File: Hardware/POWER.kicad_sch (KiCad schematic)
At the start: 91 parts, among them J201 Battery, J202 POWER IN, J203 5V_SEL, J204 E5V, SW201 START, U201 AP2112K-3.3, U203 AP2151W, U204 AP2112K-3.3, U205 AP2112K-1.8, U206 AP2112K-3.3, U207 AP2112K-3.3, U209 AP2171W

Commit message: Checkpoint
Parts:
- added R202, R210: 100K, Resistor_SMD:R_0805_2012Metric, symbol Device:R_Small
- R233: renamed from R227; value 100 -> 100R
- renumbered R202 to R203, R203 to R204, R204 to R205, R207 to R208, R208 to R209, R209 to R211, R210 to R212, R211 to R213, R212 to R214, R213 to R215, R214 to R216, R215 to R217, R217 to R218, R216 to R219, R234 to R220, R235 to R221, R236 to R222, R237 to R223, R218 to R224, R219 to R225, R220 to R226, R221 to R227, R222 to R228, R223 to R229, R225 to R230, R224 to R231, R226 to R232, R228 to R234, R229 to R235, R230 to R236, R231 to R237, R232 to R238, R233 to R239, U209 to U208
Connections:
- net D1_5V: now also R202.2, R210.2
- net D5_EN: now also R202.1
- net SERVO_5V_AUX_EN: now also R210.1

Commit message: Checkpoint
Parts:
- removed J201: Battery, Connector_PinHeader_2.54mm:PinHeader_1x07_P2.54mm_Vertical, symbol Connector_Generic:Conn_01x07
- removed R214, R216, R218, R219: 100K, Resistor_SMD:R_0805_2012Metric, symbol Device:R_Small
- removed R224, R225, R226, R227, R228: 10K, Resistor_SMD:R_0603_1608Metric, symbol Device:R_Small
- added C223, C224: 1nF, Capacitor_SMD:C_0603_1608Metric, symbol Device:C_Small
- added C? (x2): 100nF, Capacitor_SMD:C_0603_1608Metric, symbol Device:C_Small
- added R211, R220, R221: 10K, Resistor_SMD:R_0603_1608Metric, symbol Device:R_Small
- added R222, R223: 15K, Resistor_SMD:R_1206_3216Metric, symbol Device:R_Small
- added TP207, TP209: ~, TestPoint:TestPoint_Pad_D2.0mm, symbol Connector:TestPoint
- added U208, U209: ACS714xLCTR-50A, Package_SO:SOIC-8_3.9x4.9mm_P1.27mm, symbol Sensor_Current:ACS714xLCTR-50A
- R212, R213, R215: value 100K -> 10K; footprint Resistor_SMD:R_0805_2012Metric -> Resistor_SMD:R_0603_1608Metric
- renumbered C220 to C222, C221 to C225, C222 to C226, J203 to J201, J204 to J202, J202 to J203, R217 to R210, R229 to R214, R230 to R216, R231 to R217, R210 to R218, R211 to R219, R220 to R224, R221 to R225, R222 to R226, R223 to R227, R232 to R228, R233 to R229, R234 to R230, R235 to R231, R236 to R232, R237 to R233, R238 to R234, R239 to R235, TP207 to TP210, U208 to U210
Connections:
- net BATT_S2 is gone; now on net D1_5V: R213.1
- net BATT_S4 is gone; now on net MEAS_SERVO: R215.1
- net BATT_S6 is gone; now on net PWR_IN: R210.1
- net MEAS_S1 is gone; now on net SERVO_5V5: R212.1
- net MEAS_S2 is gone; now on net MEAS_D1_5V: R213.2
- net MEAS_S4 is gone; now on net GND: R215.2
- net D1_5V: now also C?.2, C?.2, U208.3 (IP-), U208.4 (IP-), U208.8 (VCC), U209.8 (VCC); no longer J201.1 (Pin_1), J201.3 (Pin_3), J201.5 (Pin_5)
- net GND: now also C223.2, C224.2, C?.1, C?.1, R222.2, R223.2, U208.5 (GND), U209.5 (GND)
- net MEAS_SERVO: now also R211.2; no longer R216.1
- net SERVO_5V5: now also R211.1, U209.3 (IP-), U209.4 (IP-)
- net BATT_S1 renamed MEAS_D5_5V
- net MEAS_D5_5V: now also R216.1
- net MEAS_S6 renamed MEAS_POWER_IN
- new net: C224.1, U209.6 (FILTER)
- new net: J201.1 (Pin_1), J201.3 (Pin_3), J201.5 (Pin_5), TP207.1, U208.1 (IP+), U208.2 (IP+)
- new net: R221.1, U209.7 (VIOUT)
- new net: C223.1, U208.6 (FILTER)
- new net: R220.1, U208.7 (VIOUT)
- new net MEAS_I_D1_5V: R220.2, R222.1
- new net MEAS_I_SERVO_5V5: R221.2, R223.1
- new net SERVO_ESC: TP209.1, U209.1 (IP+), U209.2 (IP+)
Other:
- moved on the sheet: D203, D204, D205, D206, D207, D208, J201, J202, J203, Q?, R210, R214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

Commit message: Checkpoint
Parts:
- TP201, TP202, TP203, TP204, TP205, TP206, TP207, TP208, TP209, TP210: footprint TestPoint:TestPoint_Pad_D2.0mm -> TestPoint:TestPoint_Pad_D1.0mm
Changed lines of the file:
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@@
       (effects (font (size 1.27 1.27)) hide)
     )
-    (property "Footprint" "TestPoint:TestPoint_Pad_D2.0mm" (at 109.22 213.36 0)
+    (property "Footprint" "TestPoint:TestPoint_Pad_D1.0mm" (at 109.22 213.36 0)
       (effects (font (size 1.27 1.27)) hide)
     )
@@
       (effects (font (size 1.27 1.27)) hide)
     )
-    (property "Footprint" "TestPoint:TestPoint_Pad_D2.0mm" (at 109.22 142.24 0)
+    (property "Footprint" "TestPoint:TestPoint_Pad_D1.0mm" (at 109.22 142.24 0)
       (effects (font (size 1.27 1.27)) hide)
     )
@@
       (effects (font (size 1.27 1.27)) hide)
     )
-    (property "Footprint" "TestPoint:TestPoint_Pad_D2.0mm" (at 48.26 213.36 0)
+    (property "Footprint" "TestPoint:TestPoint_Pad_D1.0mm" (at 48.26 213.36 0)
       (effects (font (size 1.27 1.27)) hide)
     )
@@
       (effects (font (size 1.27 1.27)) hide)
     )
-    (property "Footprint" "TestPoint:TestPoint_Pad_D2.0mm" (at 109.22 172.72 0)
+    (property "Footprint" "TestPoint:TestPoint_Pad_D1.0mm" (at 109.22 172.72 0)
       (effects (font (size 1.27 1.27)) hide)
     )
@@
       (effects (font (size 1.27 1.27)) hide)
     )
-    (property "Footprint" "TestPoint:TestPoint_Pad_D2.0mm" (at 154.94 109.22 0)
+    (property "Footprint" "TestPoint:TestPoint_Pad_D1.0mm" (at 154.94 109.22 0)
       (effects (font (size 1.27 1.27)) hide)
     )
@@
       (effects (font (size 1.27 1.27)) hide)
     )
-    (property "Footprint" "TestPoint:TestPoint_Pad_D2.0mm" (at 88.9 251.46 0)
+    (property "Footprint" "TestPoint:TestPoint_Pad_D1.0mm" (at 88.9 251.46 0)
       (effects (font (size 1.27 1.27)) hide)
     )
@@
       (effects (font (size 1.27 1.27)) hide)
     )
-    (property "Footprint" "TestPoint:TestPoint_Pad_D2.0mm" (at 114.3 99.06 0)
+    (property "Footprint" "TestPoint:TestPoint_Pad_D1.0mm" (at 114.3 99.06 0)
       (effects (font (size 1.27 1.27)) hide)
     )
@@
       (effects (font (size 1.27 1.27)) hide)
     )
-    (property "Footprint" "TestPoint:TestPoint_Pad_D2.0mm" (at 215.9 251.46 0)
+    (property "Footprint" "TestPoint:TestPoint_Pad_D1.0mm" (at 215.9 251.46 0)
       (effects (font (size 1.27 1.27)) hide)
     )
@@
       (effects (font (size 1.27 1.27)) hide)
     )
-    (property "Footprint" "TestPoint:TestPoint_Pad_D2.0mm" (at 152.4 53.34 0)
+    (property "Footprint" "TestPoint:TestPoint_Pad_D1.0mm" (at 152.4 53.34 0)
       (effects (font (size 1.27 1.27)) hide)
     )
@@
       (effects (font (size 1.27 1.27)) hide)
     )
-    (property "Footprint" "TestPoint:TestPoint_Pad_D2.0mm" (at 152.4 63.5 0)
-      (effects (font (size 1.27 1.27)) hide)
-    )
+    (property "Footprint" "TestPoint:TestPoint_Pad_D1.0mm" (at 152.4 63.5 0)
+      (effects (font (size 1.27 1.27)) hide)
+    )

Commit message: Checkpoint routing
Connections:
- net SERVO_5V5: now also TP209.1, U209.1 (IP+), U209.2 (IP+); no longer U209.3 (IP-), U209.4 (IP-)
- net SERVO_ESC: now also U209.3 (IP-), U209.4 (IP-); no longer TP209.1, U209.1 (IP+), U209.2 (IP+)
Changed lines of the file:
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@@
     (effects (font (size 1.27 1.27)) (justify right))
   )
-  (hierarchical_label "SERVO_ESC" (shape passive) (at 157.48 109.22 180) (fields_autoplaced)
+  (hierarchical_label "SERVO_ESC" (shape passive) (at 157.48 119.38 180) (fields_autoplaced)
     (effects (font (size 1.27 1.27)) (justify right))
   )
@@
     (effects (font (size 1.27 1.27)) (justify left))
   )
-  (hierarchical_label "SERVO_5V5" (shape passive) (at 157.48 119.38 180) (fields_autoplaced)
+  (hierarchical_label "SERVO_5V5" (shape passive) (at 157.48 109.22 180) (fields_autoplaced)
     (effects (font (size 1.27 1.27)) (justify right))
   )

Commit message: Finalize schematic and some more routing
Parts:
- R229: value 100R -> 150R; footprint Resistor_SMD:R_0805_2012Metric -> Resistor_SMD:R_0603_1608Metric
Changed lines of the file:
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@@
   (junction (at 73.66 66.04) (diameter 0) (color 0 0 0 0)
   )
+  (junction (at 160.02 68.58) (diameter 0) (color 0 0 0 0)
+  )
   (junction (at 195.58 114.3) (diameter 0) (color 0 0 0 0)
   )
@@
     (stroke (width 0) (type default))
   )
-  (wire (pts (xy 152.4 68.58) (xy 162.56 68.58))
+  (wire (pts (xy 152.4 68.58) (xy 160.02 68.58))
     (stroke (width 0) (type default))
   )
@@
     (stroke (width 0) (type default))
   )
+  (wire (pts (xy 160.02 68.58) (xy 162.56 68.58))
+    (stroke (width 0) (type default))
+  )
   (wire (pts (xy 152.4 58.42) (xy 160.02 58.42))
     (stroke (width 0) (type default))
@@
   (symbol (lib_id "power:PWR_FLAG") (at 274.32 266.7 180) (unit 1)
     (in_bom yes) (on_board yes) (dnp no) (fields_autoplaced)
-    (property "Reference" "#FLG0204" (at 274.32 268.605 0)
+    (property "Reference" "#FLG0205" (at 274.32 268.605 0)
       (effects (font (size 1.27 1.27)) hide)
     )
@@
       (project "Avionus_Flight_Controller"
         (path "/ddc7e940-0588-4587-8902-8ced9e615ace/26f6db01-be5b-4944-aca8-25d2b5bac430"
-          (reference "#FLG0204") (unit 1)
+          (reference "#FLG0205") (unit 1)
         )
       )
@@
   (symbol (lib_id "power:PWR_FLAG") (at 271.78 27.94 180) (unit 1)
     (in_bom yes) (on_board yes) (dnp no) (fields_autoplaced)
-    (property "Reference" "#FLG0203" (at 271.78 29.845 0)
+    (property "Reference" "#FLG0204" (at 271.78 29.845 0)
       (effects (font (size 1.27 1.27)) hide)
     )
@@
       (project "Avionus_Flight_Controller"
         (path "/ddc7e940-0588-4587-8902-8ced9e615ace/26f6db01-be5b-4944-aca8-25d2b5bac430"
-          (reference "#FLG0203") (unit 1)
+          (reference "#FLG0204") (unit 1)
         )
       )
@@
       (effects (font (size 1.27 1.27)) (justify left))
     )
-    (property "Value" "100R" (at 368.3 26.67 0)
+    (property "Value" "150R" (at 368.3 26.67 0)
       (effects (font (size 1.27 1.27)) (justify left))
     )
-    (property "Footprint" "Resistor_SMD:R_0805_2012Metric" (at 365.76 25.4 0)
+    (property "Footprint" "Resistor_SMD:R_0603_1608Metric" (at 365.76 25.4 0)
       (effects (font (size 1.27 1.27)) hide)
     )
@@
   (symbol (lib_id "power:PWR_FLAG") (at 271.78 25.4 0) (unit 1)
     (in_bom yes) (on_board yes) (dnp no) (fields_autoplaced)
-    (property "Reference" "#FLG0202" (at 271.78 23.495 0)
+    (property "Reference" "#FLG0203" (at 271.78 23.495 0)
       (effects (font (size 1.27 1.27)) hide)
     )
@@
       (project "Avionus_Flight_Controller"
         (path "/ddc7e940-0588-4587-8902-8ced9e615ace/26f6db01-be5b-4944-aca8-25d2b5bac430"
-          (reference "#FLG0202") (unit 1)
+          (reference "#FLG0203") (unit 1)
         )
       )
@@
         )
       )
+    )
+  )
+  (symbol (lib_id "power:PWR_FLAG") (at 160.02 68.58 180) (unit 1)
+    (in_bom yes) (on_board yes) (dnp no) (fields_autoplaced)
+    (property "Reference" "#FLG0202" (at 160.02 70.485 0)
+      (effects (font (size 1.27 1.27)) hide)
+    )
+    (property "Value" "PWR_FLAG" (at 160.02 73.66 0)
+      (effects (font (size 1.27 1.27)))
+    )
+    (property "Footprint" "" (at 160.02 68.58 0)
+      (effects (font (size 1.27 1.27)) hide)
+    )
+    (property "Datasheet" "~" (at 160.02 68.58 0)
+      (effects (font (size 1.27 1.27)) hide)
+    )
+    (pin "1")
+    (instances
+      (project "Avionus_Flight_Controller"
+        (path "/ddc7e940-0588-4587-8902-8ced9e615ace/26f6db01-be5b-4944-aca8-25d2b5bac430"
+          (reference "#FLG0202") (unit 1)
+        )
+      )

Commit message: Misc routing
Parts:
- removed TP209: ~, TestPoint:TestPoint_Pad_D1.0mm, symbol Connector:TestPoint
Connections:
- net D5_5V: now also R212.1
- net SERVO_5V5: no longer R212.1
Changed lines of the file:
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@@
   (junction (at 45.72 25.4) (diameter 0) (color 0 0 0 0)
   )
-  (junction (at 160.02 109.22) (diameter 0) (color 0 0 0 0)
-  )
   (junction (at 165.1 185.42) (diameter 0) (color 0 0 0 0)
   )
@@
     (stroke (width 0) (type default))
   )
-  (wire (pts (xy 157.48 109.22) (xy 160.02 109.22))
-    (stroke (width 0) (type default))
-  )
   (wire (pts (xy 114.3 93.98) (xy 111.76 93.98))
     (stroke (width 0) (type default))
@@
     (stroke (width 0) (type default))
   )
-  (wire (pts (xy 160.02 109.22) (xy 162.56 109.22))
+  (wire (pts (xy 157.48 109.22) (xy 162.56 109.22))
     (stroke (width 0) (type default))
   )
@@
     (effects (font (size 1.27 1.27)) (justify left))
   )
-  (hierarchical_label "SERVO_5V5" (shape passive) (at 157.48 205.74 180) (fields_autoplaced)
-    (effects (font (size 1.27 1.27)) (justify right))
-  )
   (hierarchical_label "MEAS_D2_1V8" (shape output) (at 223.52 198.12 0) (fields_autoplaced)
     (effects (font (size 1.27 1.27)) (justify left))
@@
     (effects (font (size 1.27 1.27)) (justify right))
   )
+  (hierarchical_label "D5_5V" (shape passive) (at 157.48 205.74 180) (fields_autoplaced)
+    (effects (font (size 1.27 1.27)) (justify right))
+  )
   (hierarchical_label "SERVO_ESC" (shape passive) (at 157.48 119.38 180) (fields_autoplaced)
     (effects (font (size 1.27 1.27)) (justify right))
@@
         )
       )
-    )
-  )
-  (symbol (lib_id "Connector:TestPoint") (at 160.02 109.22 0) (mirror y) (unit 1)
-    (in_bom yes) (on_board yes) (dnp no)
-    (property "Reference" "TP209" (at 157.48 105.918 0)
-      (effects (font (size 1.27 1.27)) (justify left))
-    )
-    (property "Value" "~" (at 157.48 105.918 90)
-      (effects (font (size 1.27 1.27)) hide)
-    )
-    (property "Footprint" "TestPoint:TestPoint_Pad_D1.0mm" (at 154.94 109.22 0)
-      (effects (font (size 1.27 1.27)) hide)
-    )
-    (property "Datasheet" "~" (at 154.94 109.22 0)
-      (effects (font (size 1.27 1.27)) hide)
-    )
-    (pin "1")
-    (instances
-      (project "Avionus_Flight_Controller"
-        (path "/ddc7e940-0588-4587-8902-8ced9e615ace/26f6db01-be5b-4944-aca8-25d2b5bac430"
-          (reference "TP209") (unit 1)
-        )
-      )

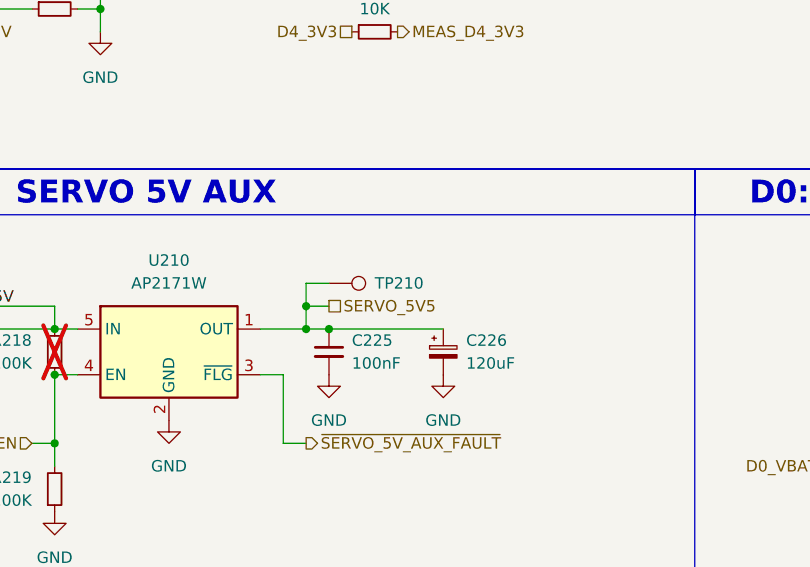
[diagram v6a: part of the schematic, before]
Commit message: Schematic layout fixes
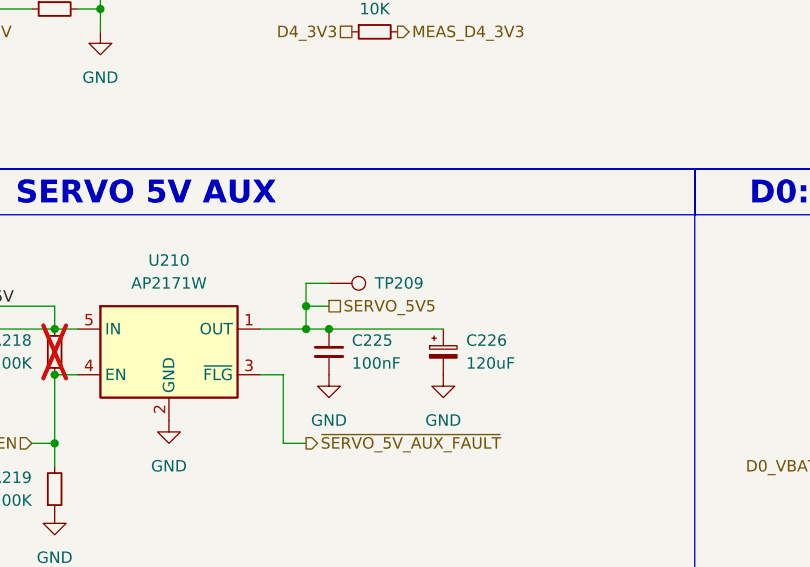
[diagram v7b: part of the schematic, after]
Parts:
- renumbered TP210 to TP209
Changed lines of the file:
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@@
   (symbol (lib_id "Connector:TestPoint") (at 215.9 246.38 270) (unit 1)
     (in_bom yes) (on_board yes) (dnp no) (fields_autoplaced)
-    (property "Reference" "TP210" (at 220.98 246.38 90)
+    (property "Reference" "TP209" (at 220.98 246.38 90)
       (effects (font (size 1.27 1.27)) (justify left))
     )
@@
       (project "Avionus_Flight_Controller"
         (path "/ddc7e940-0588-4587-8902-8ced9e615ace/26f6db01-be5b-4944-aca8-25d2b5bac430"
-          (reference "TP210") (unit 1)
+          (reference "TP209") (unit 1)
         )
       )

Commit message: Misc
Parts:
- R222, R223: value 15K -> 12K
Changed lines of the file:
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@@
       (effects (font (size 1.27 1.27)) (justify left))
     )
-    (property "Value" "15K" (at 198.12 123.19 0)
+    (property "Value" "12K" (at 198.12 123.19 0)
       (effects (font (size 1.27 1.27)) (justify left))
     )
@@
       (effects (font (size 1.27 1.27)) (justify left))
     )
-    (property "Value" "15K" (at 198.12 72.39 0)
-      (effects (font (size 1.27 1.27)) (justify left))
-    )
+    (property "Value" "12K" (at 198.12 72.39 0)
+      (effects (font (size 1.27 1.27)) (justify left))
+    )
